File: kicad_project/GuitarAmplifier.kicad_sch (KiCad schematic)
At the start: 12 parts, among them J1 NMJ6HCD2, J2 Screw_Terminal_01x02, U1 TL072CP

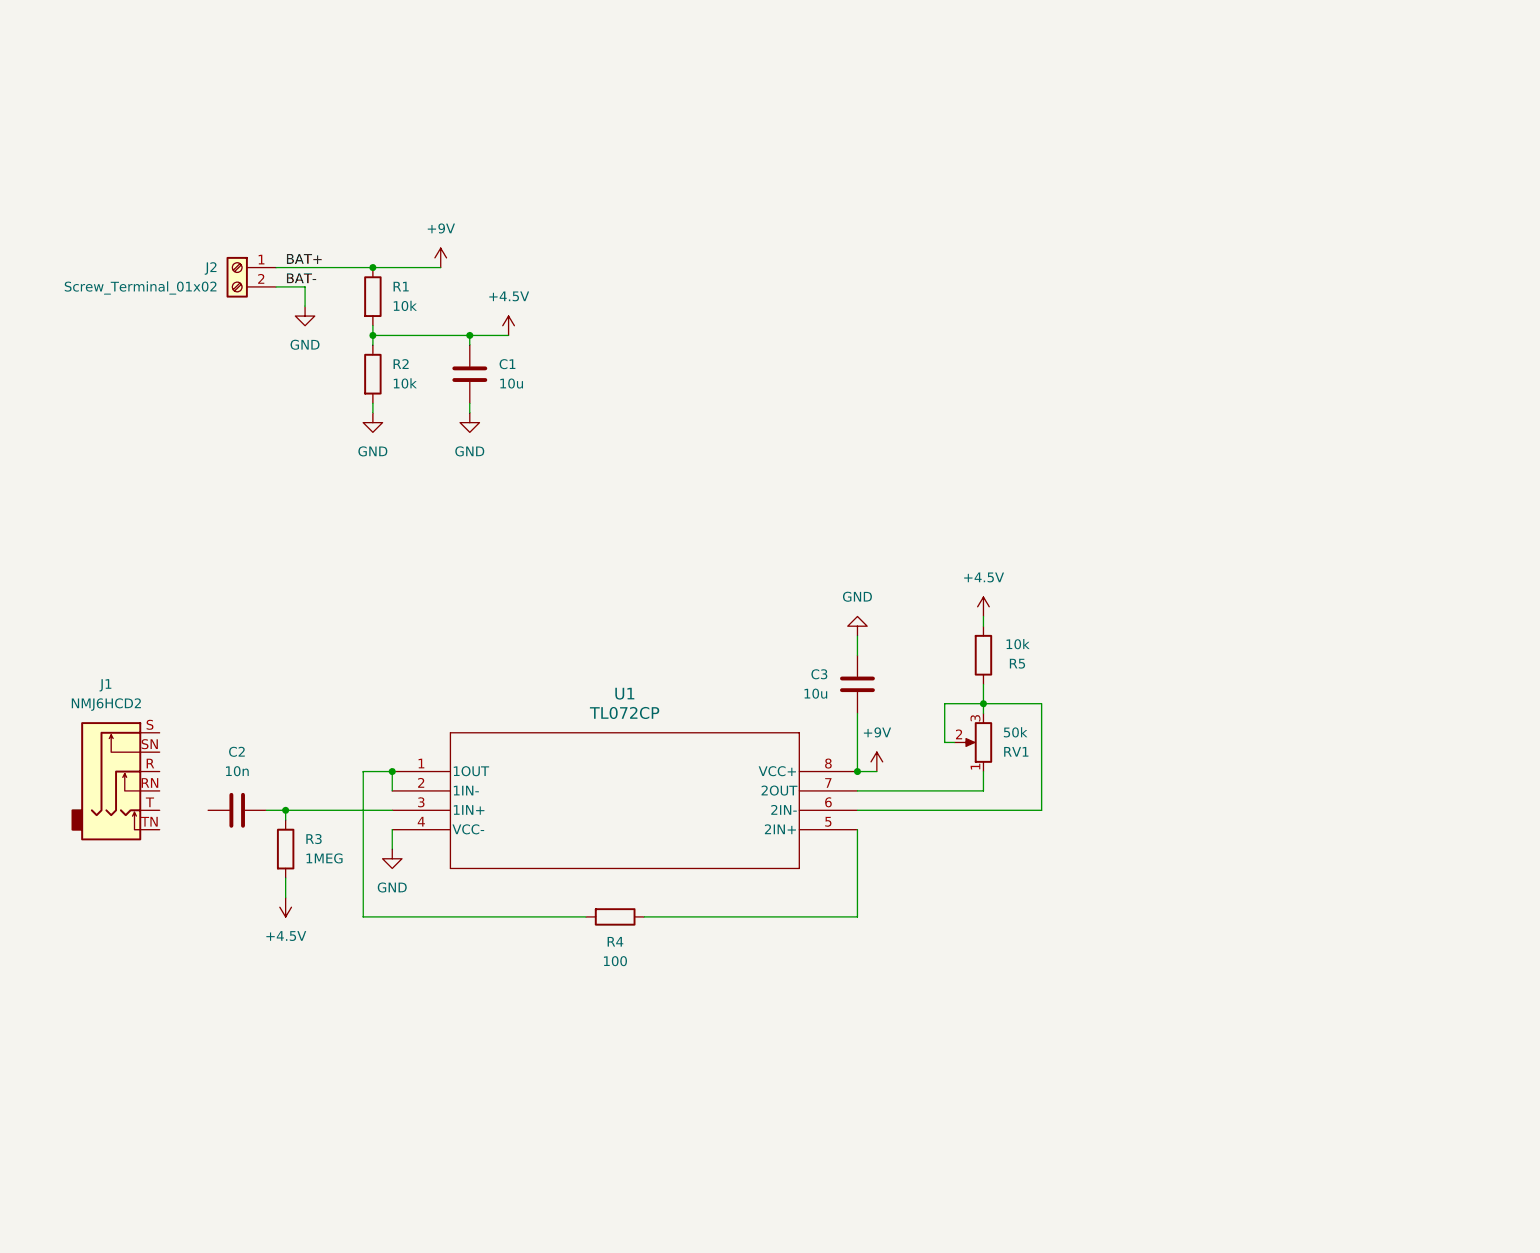
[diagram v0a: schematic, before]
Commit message: Agregando etapa de ecualizacion
Signed-off-by: RoMadrigal <rmadrigalmontes@gmail.com>
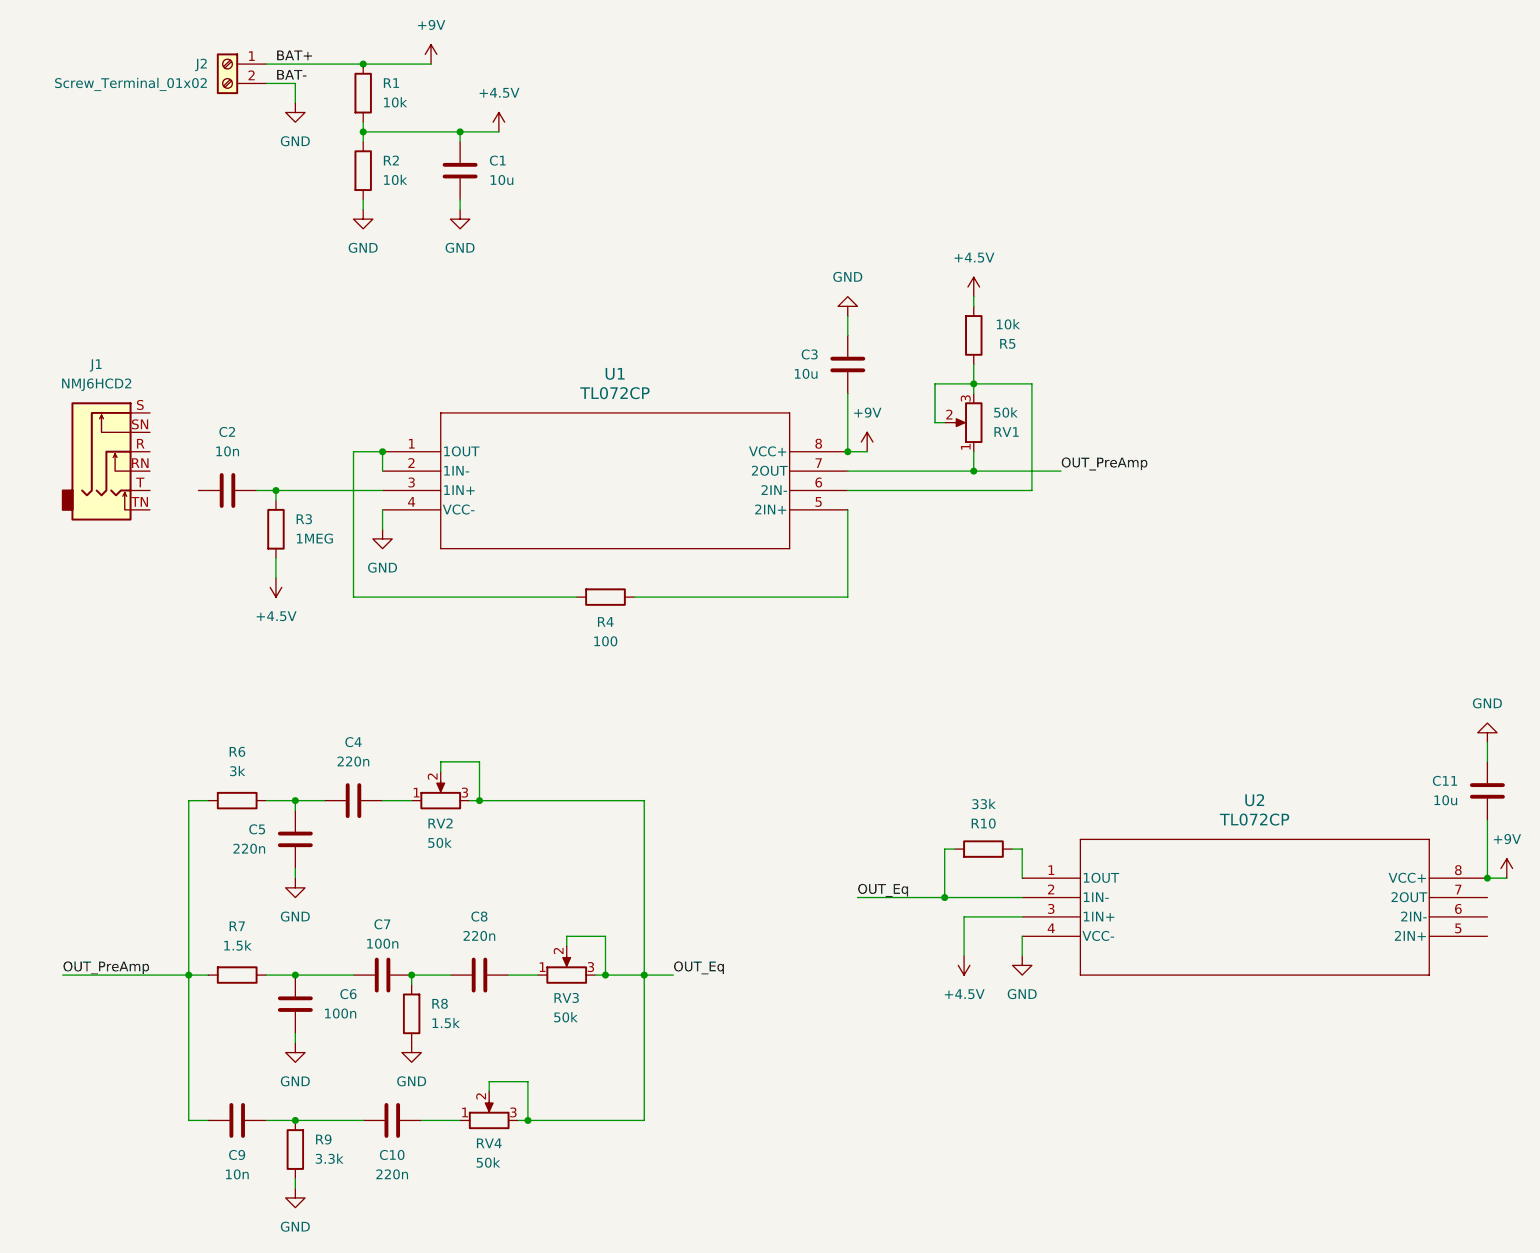
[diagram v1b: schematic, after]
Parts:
- added C10, C4, C5, C8: 220n, symbol Device:C
- added C11: 10u, Capacitor_THT:C_Disc_D7.5mm_W5.0mm_P5.00mm, symbol Device:C
- added C6, C7: 100n, symbol Device:C
- added C9: 10n, symbol Device:C
- added R10: 33k, Resistor_THT:R_Axial_DIN0207_L6.3mm_D2.5mm_P7.62mm_Horizontal, symbol Device:R
- added R6: 3k, Resistor_THT:R_Axial_DIN0207_L6.3mm_D2.5mm_P7.62mm_Horizontal, symbol Device:R
- added R7, R8: 1.5k, Resistor_THT:R_Axial_DIN0207_L6.3mm_D2.5mm_P7.62mm_Horizontal, symbol Device:R
- added R9: 3.3k, Resistor_THT:R_Axial_DIN0207_L6.3mm_D2.5mm_P7.62mm_Horizontal, symbol Device:R
- added RV2, RV3, RV4: 50k, Potentiometer_THT:Potentiometer_Vishay_T93XA_Horizontal, symbol Device:R_Potentiometer
- added U2: TL072CP, TL072CP:P8, symbol TL072CP:TL072CP
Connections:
- net +4.5V: now also U2.3 (1IN+)
- net +9V: now also C11.2, U2.8 (VCC+)
- net GND: now also C11.1, C5.1, C6.1, R8.1, R9.1, U2.4 (VCC-)
- net OUT_PreAmp: now reaches RV1.1, U1.7 (2OUT)
- net OUT_PreAmp: now also C9.2, R6.2, R7.2
- new net: C8.1, RV3.1
- new net: C10.2, C9.1, R9.2
- new net: C4.2, C5.2, R6.1
- new net: C4.1, RV2.1
- new net: C10.1, RV4.1
- new net: R10.1, U2.1 (1OUT)
- new net: C6.2, C7.2, R7.1
- new net: C7.1, C8.2, R8.2
- new net OUT_Eq: R10.2, RV2.2, RV2.3, RV3.2, RV3.3, RV4.2, RV4.3, U2.2 (1IN-)
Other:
- moved on the sheet: C1, C2, C3, J1, J2, R1, R2, R3, R4, R5, RV1, U1

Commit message: Agregando el overdrive, la etapa de salida ambas verificadas y una representación casi finalizada de la PCB
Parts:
- added C12, C13, C15, C16: 10u, Capacitor_THT:C_Disc_D7.5mm_W5.0mm_P5.00mm, symbol Device:C
- added C14: 220u, Capacitor_THT:C_Disc_D8.0mm_W5.0mm_P7.50mm, symbol Device:C
- added D1: 1N4002, Diode_THT:D_DO-41_SOD81_P10.16mm_Horizontal, symbol Diode:1N4002
- added J3: Screw_Terminal_01x02, TerminalBlock_Phoenix:TerminalBlock_Phoenix_MPT-0,5-2-2.54_1x02_P2.54mm_Horizontal, symbol Connector:Screw_Terminal_01x02
- added J4: Terminal_01x03, TerminalBlock:TerminalBlock_Xinya_XY308-2.54-3P_1x03_P2.54mm_Horizontal, symbol Connector:Screw_Terminal_01x03
- added R11: 175, Resistor_THT:R_Axial_DIN0207_L6.3mm_D2.5mm_P7.62mm_Horizontal, symbol Device:R
- added R12: 10k, Resistor_THT:R_Axial_DIN0207_L6.3mm_D2.5mm_P7.62mm_Horizontal, symbol Device:R
- added RV5: 50k, Potentiometer_THT:Potentiometer_Vishay_T93XA_Horizontal, symbol Device:R_Potentiometer
- added U3: LM386, Package_DIP:DIP-8_W7.62mm, symbol Amplifier_Audio:LM386
- C10, C4, C5, C8: footprint (none) -> Capacitor_THT:C_Disc_D8.0mm_W5.0mm_P7.50mm
- C2, C6, C7, C9: footprint (none) -> Capacitor_THT:C_Disc_D7.5mm_W5.0mm_P5.00mm
- U1, U2: footprint TL072CP:P8 -> Huella:TL072Cp; Description_1 (none) -> Dual Low-Noise JFET-Input General-Purpose Operational Ampli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; Height (none) -> 5.08; Manufacturer_Name (none) -> Texas Instruments; Manufacturer_Part_Number (none) -> TL072CP; Mouser Part Number (none) -> 595-TL072CP; Mouser Price/Stock (none) -> https://www.mouser.co.uk/ProductDetail/Texas-Instruments/TL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
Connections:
- net +9V: now also C15.2, U3.6 (V+)
- net GND: now also J1.R, J1.RN, J1.S, J1.SN, J1.TN, C12.1, C13.2, C15.1, R11.2, RV5.3, U3.1 (GAIN), U3.2 (-), U3.4 (GND), U3.8 (GAIN)
- net OUT_Eq: now also U2.5 (2IN+), J4.3 (Pin_3)
- net at U2.6 (2IN-): now also D1.1 (K), R11.1
- net OUT_OverD: now reaches U2.7 (2OUT)
- net OUT_OverD: now also D1.2 (A), J4.1 (Pin_1)
- net at J1.T: now also C2.2
- new net: C16.1, J4.2 (Pin_2)
- new net: C16.2, RV5.1
- new net: RV5.2, U3.3 (+)
- new net: C14.1, R12.2, U3.5
- new net: C12.2, U3.7 (BYPASS)
- new net: C13.1, R12.1
- new net System_Out: C14.2, J3.2 (Pin_2)
- no-connect marks 0 -> 1
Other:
- note added: "BAT +"
- note added: "BAT -"
- company: (none) -> University of Costa Rica
- moved on the sheet: C10, C11, C2, C3, C4, C5, C6, C7, C8, C9, J1, R10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

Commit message: Realizando acomodo final en el esquematico y PCB
Signed-off-by: RoMadrigal <rmadrigalmontes@gmail.com>
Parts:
- removed U1, U2: TL072CP, Huella:TL072Cp, symbol TL072CP:TL072CP
- added U1, U2: TL072CP, Package_DIP:DIP-8_W7.62mm, symbol TL072CP2:TL072CP
- R12: value 10k -> 10
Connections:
- net +4.5V: now also U2.3 (1IN+)
- net +9V: now also U1.8 (VCC+), U2.8 (VCC+)
- net GND: now also J3.1 (Pin_1), U1.4 (VCC-), U2.4 (VCC-); no longer U3.1 (GAIN), U3.8 (GAIN)
- net OUT_Eq: now also U2.2 (1IN-); no longer J4.3 (Pin_3)
- net OUT_OverD: now also U2.7 (2OUT)
- net OUT_PreAmp: now also U1.7 (2OUT)
- net OUT_Clean: now reaches R10.1
- net OUT_Clean: now also J4.3 (Pin_3), U2.1 (1OUT), U2.5 (2IN+)
- net at D1.1 (K), R11.1: now also U2.6 (2IN-)
- net at C2.1, R3.1: now also U1.3 (1IN+)
- net at R4.2: now also U1.1 (1OUT), U1.2 (1IN-)
- net at R4.1: now also U1.5 (2IN+)
- net at R5.1, RV1.2, RV1.3: now also U1.6 (2IN-)
- no-connect marks 1 -> 2
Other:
- moved on the sheet: C1, C10, C11, C12, C13, C14, C15, C16, C2, C3, C4, C5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

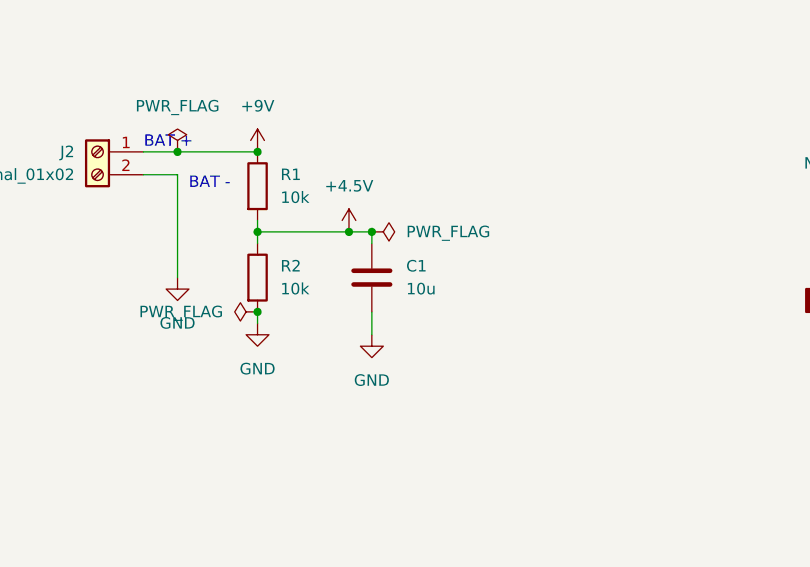
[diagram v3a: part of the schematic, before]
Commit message: Definiendo las capas de alimentacion y tierra en la PCB
Signed-off-by: RoMadrigal <rmadrigalmontes@gmail.com>
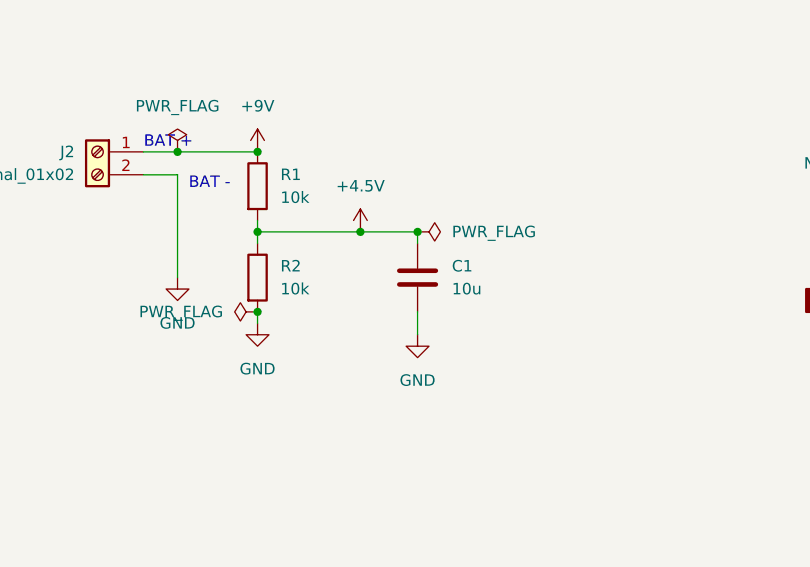
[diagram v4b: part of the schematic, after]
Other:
- moved on the sheet: C1
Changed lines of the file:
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@@
 	)
 	(junction
-		(at 69.85 48.26)
+		(at 71.12 48.26)
 		(diameter 0)
 		(color 0 0 0 0)
@@
 	)
 	(junction
-		(at 72.39 48.26)
+		(at 77.47 48.26)
 		(diameter 0)
 		(color 0 0 0 0)
@@
 	(wire
 		(pts
-			(xy 59.69 48.26) (xy 69.85 48.26)
+			(xy 59.69 48.26) (xy 71.12 48.26)
 		)
 		(stroke
@@
 	(wire
 		(pts
-			(xy 72.39 48.26) (xy 72.39 49.53)
+			(xy 77.47 48.26) (xy 77.47 49.53)
 		)
 		(stroke
@@
 	(wire
 		(pts
-			(xy 69.85 48.26) (xy 72.39 48.26)
+			(xy 71.12 48.26) (xy 77.47 48.26)
 		)
 		(stroke
@@
 	(wire
 		(pts
-			(xy 72.39 59.69) (xy 72.39 57.15)
+			(xy 77.47 59.69) (xy 77.47 57.15)
 		)
 		(stroke
@@
 	(symbol
 		(lib_id "power:+4V")
-		(at 69.85 48.26 0)
+		(at 71.12 48.26 0)
 		(unit 1)
 		(exclude_from_sim no)
@@
 		(fields_autoplaced yes)
 		(property "Reference" "#PWR07"
-			(at 69.85 52.07 0)
+			(at 71.12 52.07 0)
 			(effects
 				(font
@@
 		)
 		(property "Value" "+4.5V"
-			(at 69.85 43.18 0)
+			(at 71.12 43.18 0)
 			(effects
 				(font
@@
 		)
 		(property "Footprint" ""
-			(at 69.85 48.26 0)
+			(at 71.12 48.26 0)
 			(effects
 				(font
@@
 		)
 		(property "Datasheet" ""
-			(at 69.85 48.26 0)
+			(at 71.12 48.26 0)
 			(effects
 				(font
@@
 		)
 		(property "Description" "Power symbol creates a global label with name \"+4V\""
-			(at 69.85 48.26 0)
+			(at 71.12 48.26 0)
 			(effects
 				(font
@@
 	(symbol
 		(lib_id "power:PWR_FLAG")
-		(at 72.39 48.26 270)
+		(at 77.47 48.26 270)
 		(unit 1)
 		(exclude_from_sim no)
@@
 		(fields_autoplaced yes)
 		(property "Reference" "#FLG02"
-			(at 74.295 48.26 0)
+			(at 79.375 48.26 0)
 			(effects
 				(font
@@
 		)
 		(property "Value" "PWR_FLAG"
-			(at 76.2 48.2599 90)
+			(at 81.28 48.2599 90)
 			(effects
 				(font
@@
 		)
 		(property "Footprint" ""
-			(at 72.39 48.26 0)
+			(at 77.47 48.26 0)
 			(effects
 				(font
@@
 		)
 		(property "Datasheet" "~"
-			(at 72.39 48.26 0)
+			(at 77.47 48.26 0)
 			(effects
 				(font
@@
 		)
 		(property "Description" "Special symbol for telling ERC where power comes from"
-			(at 72.39 48.26 0)
+			(at 77.47 48.26 0)
 			(effects
 				(font
@@
 	(symbol
 		(lib_id "power:GND")
-		(at 72.39 59.69 0)
+		(at 77.47 59.69 0)
 		(unit 1)
 		(exclude_from_sim no)
@@
 		(fields_autoplaced yes)
 		(property "Reference" "#PWR028"
-			(at 72.39 66.04 0)
+			(at 77.47 66.04 0)
 			(effects
 				(font
@@
 		)
 		(property "Value" "GND"
-			(at 72.39 64.77 0)
+			(at 77.47 64.77 0)
 			(effects
 				(font
@@
 		)
 		(property "Footprint" ""
-			(at 72.39 59.69 0)
+			(at 77.47 59.69 0)
 			(effects
 				(font
@@
 		)
 		(property "Datasheet" ""
-			(at 72.39 59.69 0)
+			(at 77.47 59.69 0)
 			(effects
 				(font
@@
 		)
 		(property "Description" "Power symbol creates a global label with name \"GND\" , ground"
-			(at 72.39 59.69 0)
+			(at 77.47 59.69 0)
 			(effects
 				(font
@@
 	(symbol
 		(lib_id "Device:C")
-		(at 72.39 53.34 0)
+		(at 77.47 53.34 0)
 		(unit 1)
 		(exclude_from_sim no)
@@
 		(fields_autoplaced yes)
 		(property "Reference" "C1"
-			(at 76.2 52.0699 0)
+			(at 81.28 52.0699 0)
 			(effects
 				(font
@@
 		)
 		(property "Value" "10u"
-			(at 76.2 54.6099 0)
+			(at 81.28 54.6099 0)
 			(effects
 				(font
@@
 		)
 		(property "Footprint" "Capacitor_THT:C_Disc_D7.5mm_W5.0mm_P5.00mm"
-			(at 73.3552 57.15 0)
+			(at 78.4352 57.15 0)
 			(effects
 				(font
@@
 		)
 		(property "Datasheet" "~"
-			(at 72.39 53.34 0)
+			(at 77.47 53.34 0)
 			(effects
 				(font
@@
 		)
 		(property "Description" "Unpolarized capacitor"
-			(at 72.39 53.34 0)
+			(at 77.47 53.34 0)
 			(effects
 				(font

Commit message: Agregando el enrutamiento final y una reconfiguración de la placa
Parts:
- U1, U2: symbol TL072CP2:TL072CP -> TL072CP:TL072CP
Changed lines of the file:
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@@
 	)
 	(symbol
-		(lib_id "TL072CP2:TL072CP")
+		(lib_id "TL072CP:TL072CP")
 		(at 166.37 119.38 0)
 		(unit 1)
@@
 	)
 	(symbol
-		(lib_id "TL072CP2:TL072CP")
+		(lib_id "TL072CP:TL072CP")
 		(at 162.56 49.53 0)
 		(unit 1)

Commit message: Terminando de rellenar la capa inferior y ajustando las huellas de los conectores
Signed-off-by: RoMadrigal <rmadrigalmontes@gmail.com>
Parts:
- J2, J3: footprint TerminalBlock_Phoenix:TerminalBlock_Phoenix_MPT-0,5-2-2.54_1x02_P2.54mm_Horizontal -> TerminalBlock:TerminalBlock_bornier-2_P5.08mm
- J4: footprint TerminalBlock:TerminalBlock_Xinya_XY308-2.54-3P_1x03_P2.54mm_Horizontal -> TerminalBlock:TerminalBlock_bornier-3_P5.08mm
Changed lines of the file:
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@@
 			)
 		)
-		(property "Footprint" "TerminalBlock:TerminalBlock_Xinya_XY308-2.54-3P_1x03_P2.54mm_Horizontal"
+		(property "Footprint" "TerminalBlock:TerminalBlock_bornier-3_P5.08mm"
 			(at 274.32 106.68 0)
 			(effects
@@
 			)
 		)
-		(property "Footprint" "TerminalBlock_Phoenix:TerminalBlock_Phoenix_MPT-0,5-2-2.54_1x02_P2.54mm_Horizontal"
+		(property "Footprint" "TerminalBlock:TerminalBlock_bornier-2_P5.08mm"
 			(at 354.33 123.19 0)
 			(effects
@@
 			)
 		)
-		(property "Footprint" "TerminalBlock_Phoenix:TerminalBlock_Phoenix_MPT-0,5-2-2.54_1x02_P2.54mm_Horizontal"
+		(property "Footprint" "TerminalBlock:TerminalBlock_bornier-2_P5.08mm"
 			(at 41.91 39.37 0)
 			(effects

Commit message: Reasignando huella de los potenciometros
Signed-off-by: RoMadrigal <rmadrigalmontes@gmail.com>
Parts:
- RV1, RV2, RV3, RV4, RV5: footprint Potentiometer_THT:Potentiometer_Vishay_T93XA_Horizontal -> Potentiometer_THT:Potentiometer_Piher_PC-16_Single_Horizontal
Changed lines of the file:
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@@
 			)
 		)
-		(property "Footprint" "Potentiometer_THT:Potentiometer_Vishay_T93XA_Horizontal"
+		(property "Footprint" "Potentiometer_THT:Potentiometer_Piher_PC-16_Single_Horizontal"
 			(at 88.9 124.46 0)
 			(effects
@@
 			)
 		)
-		(property "Footprint" "Potentiometer_THT:Potentiometer_Vishay_T93XA_Horizontal"
+		(property "Footprint" "Potentiometer_THT:Potentiometer_Piher_PC-16_Single_Horizontal"
 			(at 240.03 45.72 0)
 			(effects
@@
 			)
 		)
-		(property "Footprint" "Potentiometer_THT:Potentiometer_Vishay_T93XA_Horizontal"
+		(property "Footprint" "Potentiometer_THT:Potentiometer_Piher_PC-16_Single_Horizontal"
 			(at 289.56 118.11 0)
 			(effects
@@
 			)
 		)
-		(property "Footprint" "Potentiometer_THT:Potentiometer_Vishay_T93XA_Horizontal"
+		(property "Footprint" "Potentiometer_THT:Potentiometer_Piher_PC-16_Single_Horizontal"
 			(at 78.74 143.51 0)
 			(effects
@@
 			)
 		)
-		(property "Footprint" "Potentiometer_THT:Potentiometer_Vishay_T93XA_Horizontal"
+		(property "Footprint" "Potentiometer_THT:Potentiometer_Piher_PC-16_Single_Horizontal"
 			(at 72.39 101.6 0)
 			(effects
